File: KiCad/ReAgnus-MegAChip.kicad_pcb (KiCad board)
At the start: 4 copper layers, 78 x 49 mm, 53 parts, among them J1 Conn_01x02, J2 Conn_02x05_Odd_Even, J3 Conn_02x02_Odd_Even, J4 Conn_01x01, U1 GW1NR-UV9LQ144P, U10 74LVC245A, U11 PLCC-84-Plug, U12 Agnus_TH_plug_pins, U2 LM1117-3.3, U3 TPS73643DBV, U4 SN74CBT16210, U5 SN74CBT16210, U6 SN74CBT16210, U7 SN74CBT16210, U8 74LVC1G07, U9 74LVC1GX04, Y1 CL=16pF

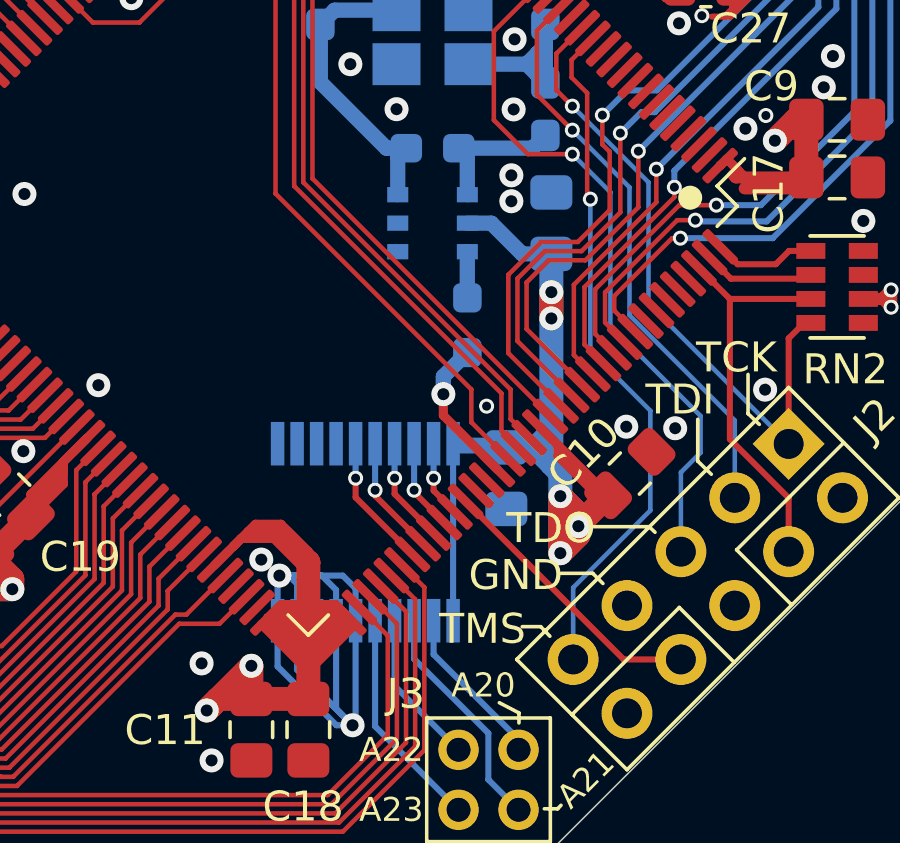
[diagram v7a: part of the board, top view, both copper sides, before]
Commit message: Assigned DIR-signal to FPGA from U10 (74LVC245)
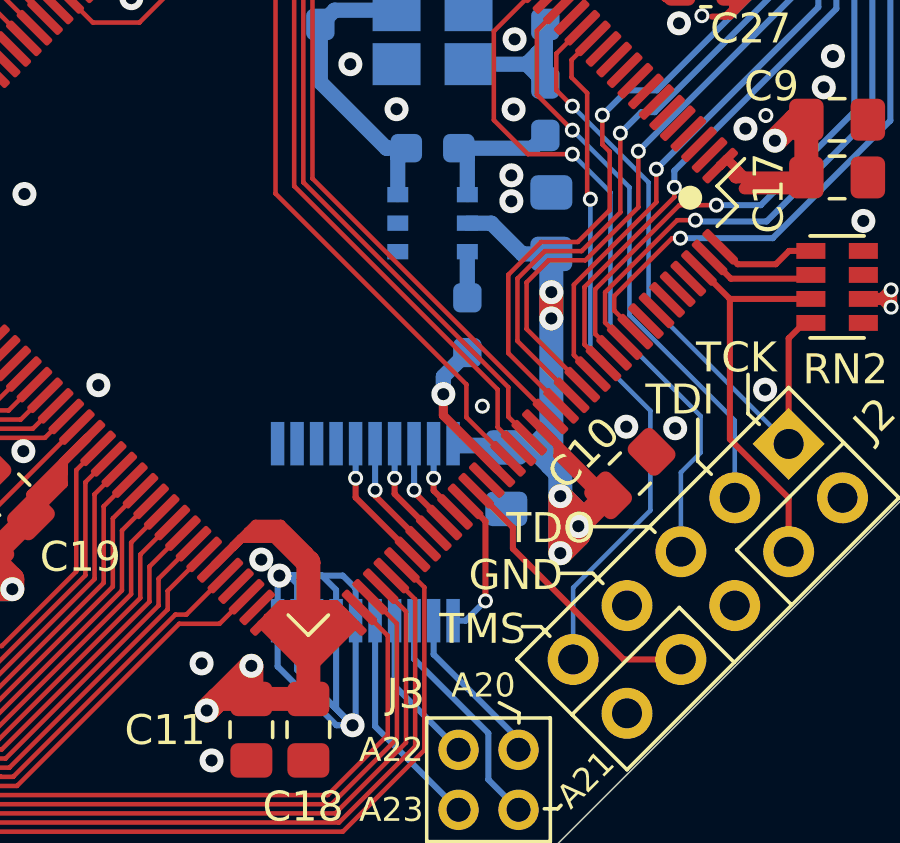
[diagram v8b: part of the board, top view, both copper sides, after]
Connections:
- U1 pad 120: JP1 -> DIR
- U1 pad 121: Net-(U1-Pad121) -> JP1
- U10 pad 1: 3V3 -> DIR
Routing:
- net 3V3: track 233.5 -> 227.6 mm
- net DIR: track 0.00 -> 4.94 mm, vias 0 -> 1
